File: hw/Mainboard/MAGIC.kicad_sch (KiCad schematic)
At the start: 17 parts, among them U18 SN74LVC4245APWR, U19 SN74LVC4245APWR, U20 SN74LVC4245APWR

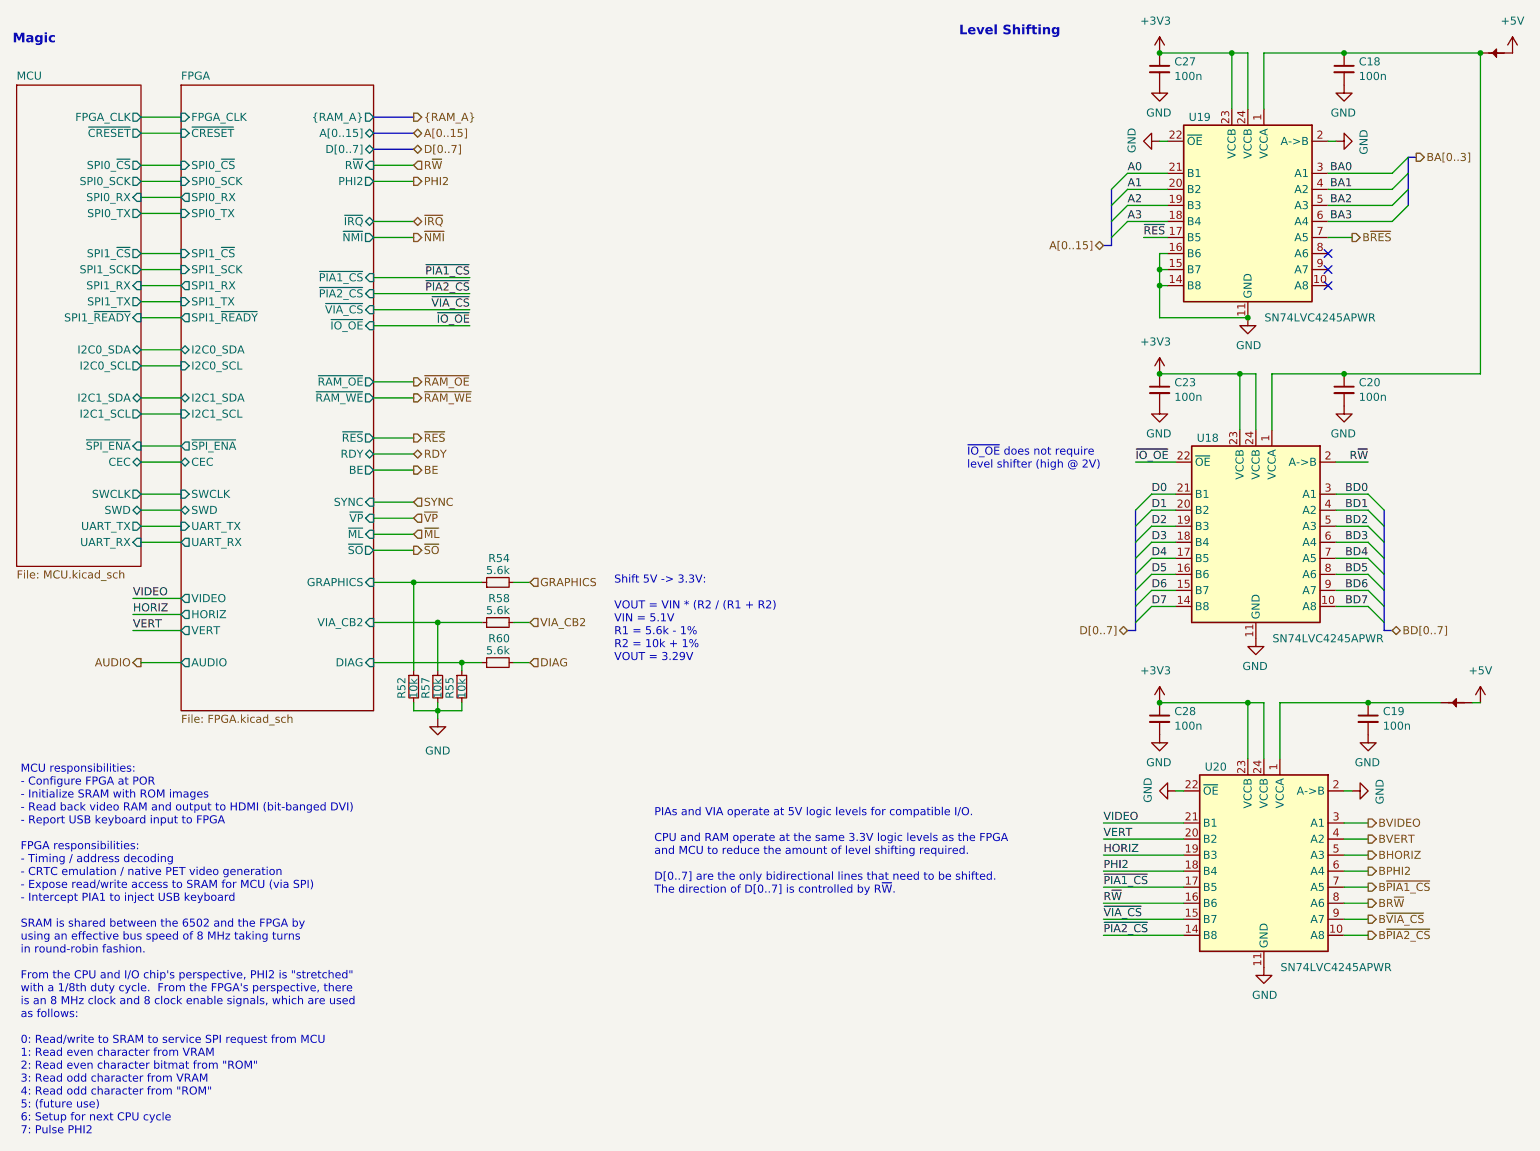
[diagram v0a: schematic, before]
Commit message: hw: 9V DC plug on left edge, change default track size
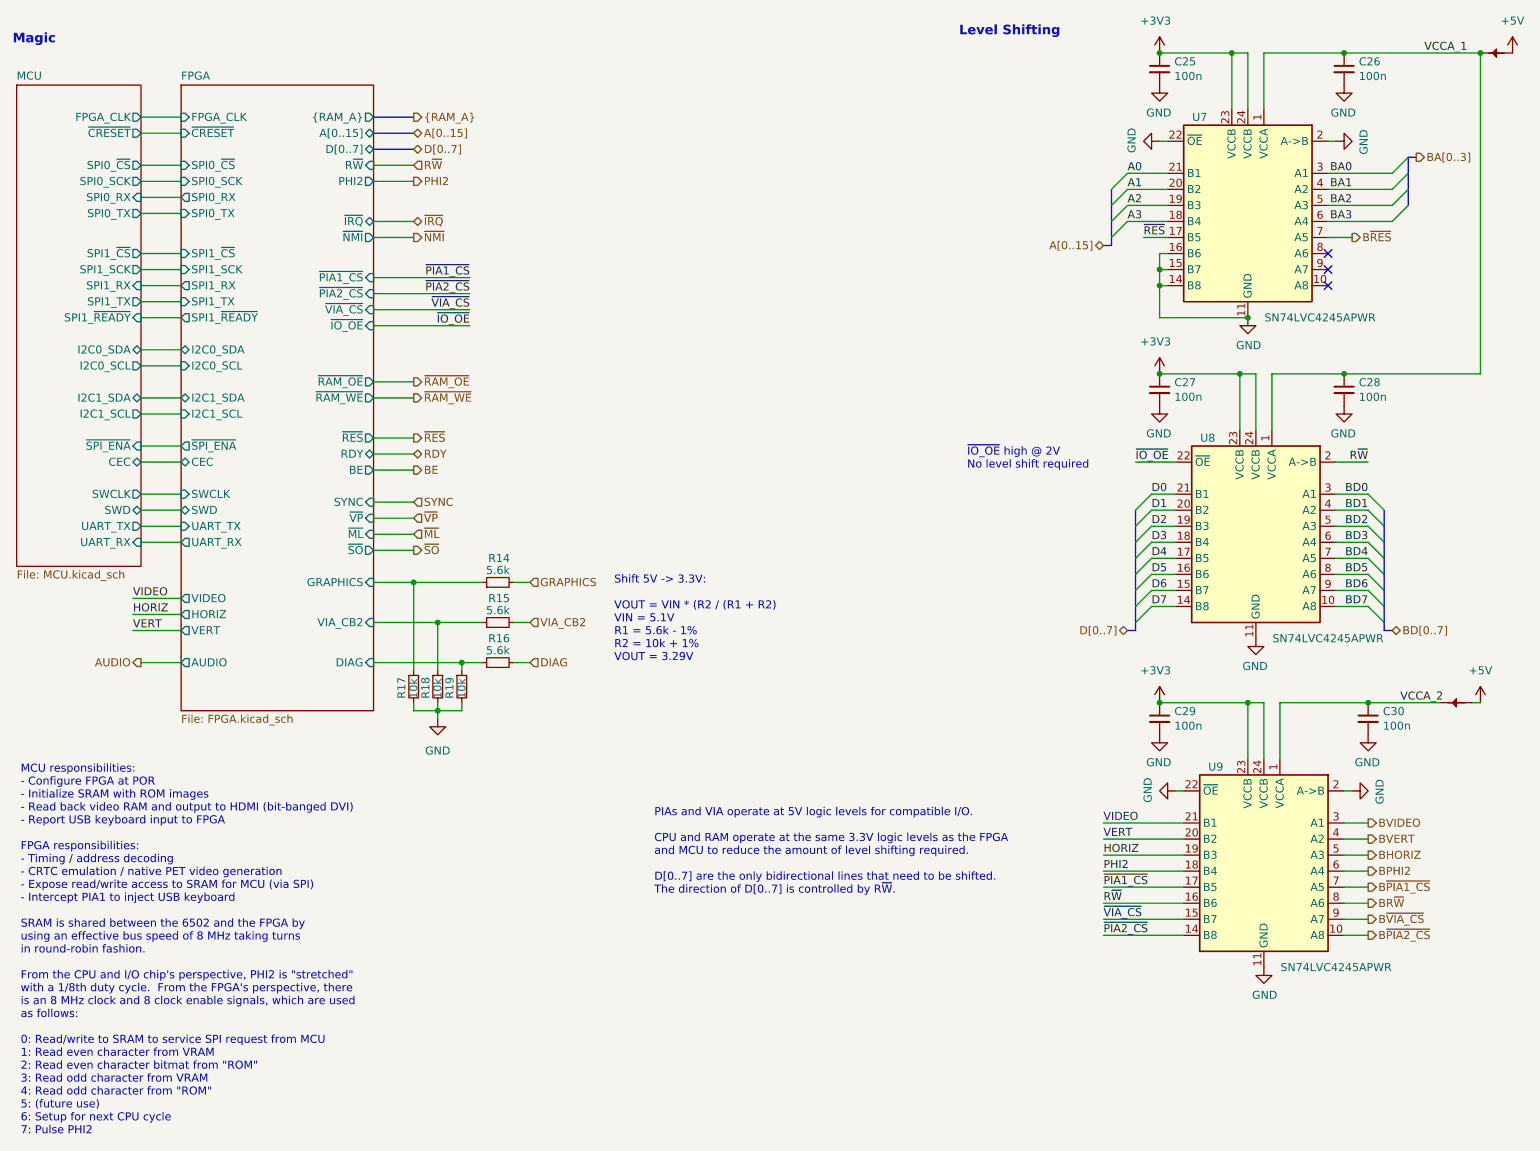
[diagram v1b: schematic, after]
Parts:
- renumbered C27 to C25, C18 to C26, C23 to C27, C20 to C28, C28 to C29, C19 to C30, PT12 to PT13, PT13 to PT14, R54 to R14, R58 to R15, R60 to R16, R52 to R17, R57 to R18, R55 to R19, U19 to U7, U18 to U8, U20 to U9
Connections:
- net VCCA_1: now reaches C26.1, C28.1, PT13.2, U7.1 (VCCA), U8.1 (VCCA)
- net VCCA_2: now reaches C30.1, PT14.2, U9.1 (VCCA)
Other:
- note added: "~{IO_OE} high @ 2V No level shift required"
- note removed: "~{IO_OE} does not require level shifter (high @ 2V)"

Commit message: hw: fill, routing, and silk touchups (wip)
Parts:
- added C88: 1u, Capacitor_SMD:C_0402_1005Metric, symbol Device:C_Small
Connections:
- net +3V3: now also C88.1
- net GND: now also C88.2
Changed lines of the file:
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@@
   (junction (at 240.03 123.19) (diameter 0) (color 0 0 0 0)
+  )
+  (junction (at 207.01 25.4) (diameter 0) (color 0 0 0 0)
   )
   (no_connect (at 233.68 52.07))
@@
     (stroke (width 0) (type default) (color 0 0 0 0))
   )
+  (wire (pts (xy 199.39 25.4) (xy 207.01 25.4))
+    (stroke (width 0) (type default) (color 0 0 0 0))
+  )
   (wire (pts (xy 208.28 41.91) (xy 201.93 41.91))
     (stroke (width 0) (type default) (color 0 0 0 0))
@@
   )
   (bus (pts (xy 246.38 36.83) (xy 246.38 39.37))
+    (stroke (width 0) (type default) (color 0 0 0 0))
+  )
+  (wire (pts (xy 199.39 20.32) (xy 207.01 20.32))
     (stroke (width 0) (type default) (color 0 0 0 0))
   )
@@
       (effects (font (size 1.27 1.27)) hide)
     )
+    (pin "1")
+    (pin "2")
+  )
+  (symbol (lib_id "Device:C_Small") (at 199.39 22.86 0) (unit 1)
+    (in_bom yes) (on_board yes)
+    (property "Reference" "C88" (id 0) (at 201.7268 21.6916 0)
+      (effects (font (size 1.27 1.27)) (justify left))
+    )
+    (property "Value" "1u" (id 1) (at 201.7268 24.003 0)
+      (effects (font (size 1.27 1.27)) (justify left))
+    )
+    (property "Footprint" "Capacitor_SMD:C_0402_1005Metric" (id 2) (at 199.39 22.86 0)
+      (effects (font (size 1.27 1.27)) hide)
+    )
+    (property "Datasheet" "https://datasheet.lcsc.com/lcsc/2304140030_Samsung-Electro-Mechanics-CL05A105KA5NQNC_C52923.pdf" (id 3) (at 199.39 22.86 0)
+      (effects (font (size 1.27 1.27)) hide)
+    )
+    (property "LCSC" "C52923" (id 4) (at 199.39 22.86 0)
+      (effects (font (size 1.27 1.27)) hide)
+    )

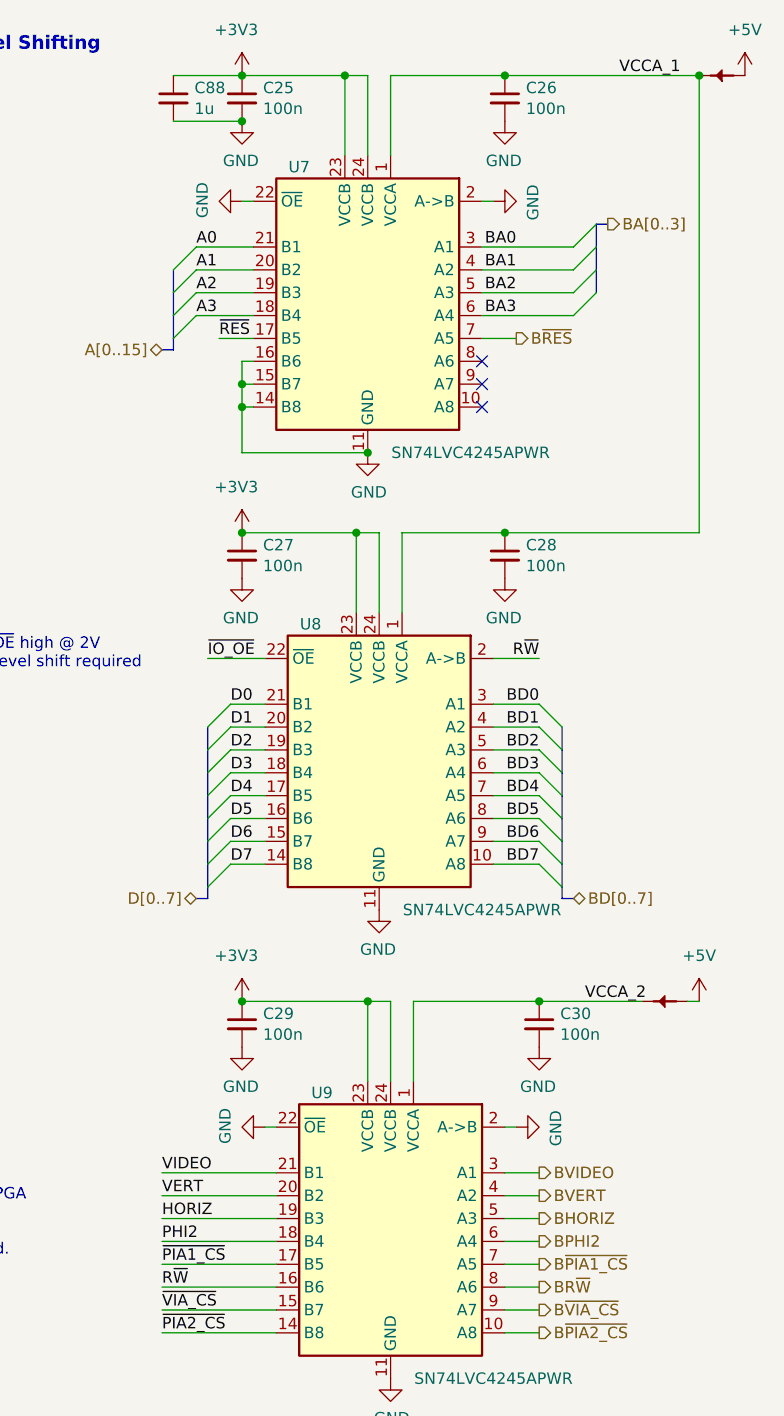
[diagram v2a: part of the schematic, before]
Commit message: hw: routing touchups (wip)
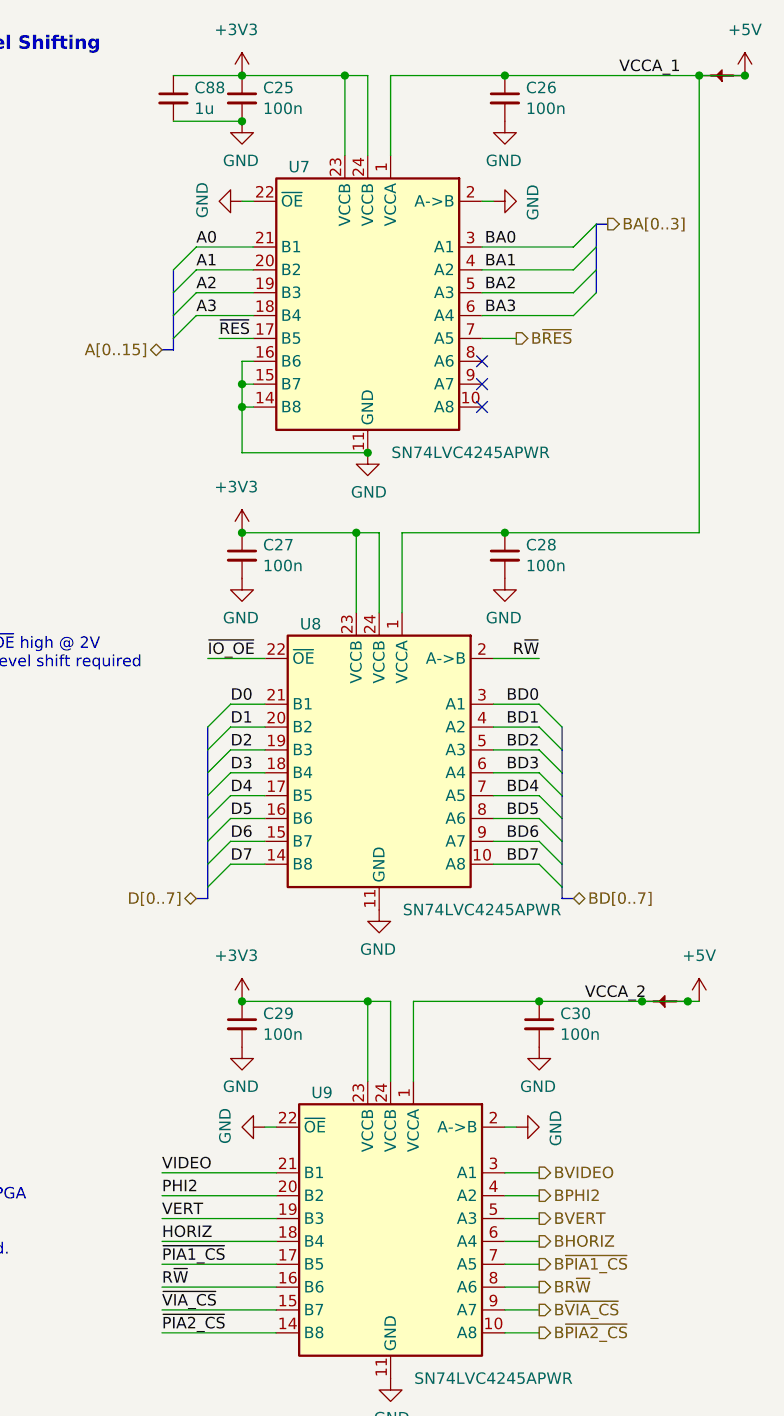
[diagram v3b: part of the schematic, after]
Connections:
- net VCCA_1 is gone; now on net +5V: C26.1, C28.1, PT13.2, U7.1 (VCCA), U8.1 (VCCA)
- net VCCA_2 is gone; now on net +5V: C30.1, PT14.2, U9.1 (VCCA)
- net BHORIZ: now also U9.6 (A4); no longer U9.5 (A3)
- net BPHI2: now also U9.4 (A2); no longer U9.6 (A4)
- net BVERT: now also U9.5 (A3); no longer U9.4 (A2)
- net HORIZ: now also U9.18 (B4); no longer U9.19 (B3)
- net PHI2: now also U9.20 (B2); no longer U9.18 (B4)
- net VERT: now also U9.19 (B3); no longer U9.20 (B2)
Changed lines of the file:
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@@
   (junction (at 207.01 57.15) (diameter 0) (color 0 0 0 0)
   )
+  (junction (at 262.89 20.32) (diameter 0) (color 0 0 0 0)
+  )
   (junction (at 220.98 62.23) (diameter 0) (color 0 0 0 0)
   )
   (junction (at 92.71 124.46) (diameter 0) (color 0 0 0 0)
   )
+  (junction (at 251.46 123.19) (diameter 0) (color 0 0 0 0)
+  )
   (junction (at 207.01 71.12) (diameter 0) (color 0 0 0 0)
   )
@@
   )
   (junction (at 96.52 116.84) (diameter 0) (color 0 0 0 0)
+  )
+  (junction (at 256.54 123.19) (diameter 0) (color 0 0 0 0)
   )
   (junction (at 219.71 71.12) (diameter 0) (color 0 0 0 0)
@@
     (stroke (width 0) (type default) (color 0 0 0 0))
   )
+  (wire (pts (xy 257.81 20.32) (xy 262.89 20.32))
+    (stroke (width 0) (type default) (color 0 0 0 0))
+  )
   (wire (pts (xy 45.72 95.25) (xy 52.07 95.25))
     (stroke (width 0) (type default) (color 0 0 0 0))
@@
   )
   (wire (pts (xy 207.01 57.15) (xy 208.28 57.15))
+    (stroke (width 0) (type default) (color 0 0 0 0))
+  )
+  (wire (pts (xy 251.46 123.19) (xy 256.54 123.19))
     (stroke (width 0) (type default) (color 0 0 0 0))
   )
@@
     (effects (font (size 1.27 1.27)) (justify left bottom))
   )
-  (label "PHI2" (at 198.12 149.86 0)
+  (label "PHI2" (at 198.12 144.78 0)
     (effects (font (size 1.27 1.27)) (justify left bottom))
   )
@@
     (effects (font (size 1.27 1.27)) (justify left bottom))
   )
-  (label "HORIZ" (at 198.12 147.32 0)
+  (label "HORIZ" (at 198.12 149.86 0)
     (effects (font (size 1.27 1.27)) (justify left bottom))
   )
@@
     (effects (font (size 1.27 1.27)) (justify left bottom))
   )
-  (label "VERT" (at 198.12 144.78 0)
+  (label "VERT" (at 198.12 147.32 0)
     (effects (font (size 1.27 1.27)) (justify left bottom))
   )
@@
     (effects (font (size 1.27 1.27)) (justify left))
   )
-  (hierarchical_label "BHORIZ" (shape output) (at 240.03 147.32 0)
+  (hierarchical_label "BHORIZ" (shape output) (at 240.03 149.86 0)
     (effects (font (size 1.27 1.27)) (justify left))
   )
@@
     (effects (font (size 1.27 1.27)) (justify left))
   )
-  (hierarchical_label "BVERT" (shape output) (at 240.03 144.78 0)
+  (hierarchical_label "BVERT" (shape output) (at 240.03 147.32 0)
     (effects (font (size 1.27 1.27)) (justify left))
   )
@@
     (effects (font (size 1.27 1.27)) (justify left))
   )
-  (hierarchical_label "BPHI2" (shape output) (at 240.03 149.86 0)
-    (effects (font (size 1.27 1.27)) (justify left))
-  )
+  (hierarchical_label "BPHI2" (shape output) (at 240.03 144.78 0)
+    (effects (font (size 1.27 1.27)) (justify left))
+  )

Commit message: hw: caps & logos (wip)
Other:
- title: CBM PET Mainboard Replacement -> EconoPET 40/8096
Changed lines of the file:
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@@
   (paper "A")
   (title_block
-    (title "CBM PET Mainboard Replacement")
+    (title "EconoPET 40/8096")
+    (date "2023-10-01")
+    (rev "A")
   )
   (junction (at 218.44 20.32) (diameter 0) (color 0 0 0 0)
